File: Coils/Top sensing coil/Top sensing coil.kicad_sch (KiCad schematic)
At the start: 6 parts, among them J1 Conn_01x02_Pin, J2 Conn_01x02_Socket

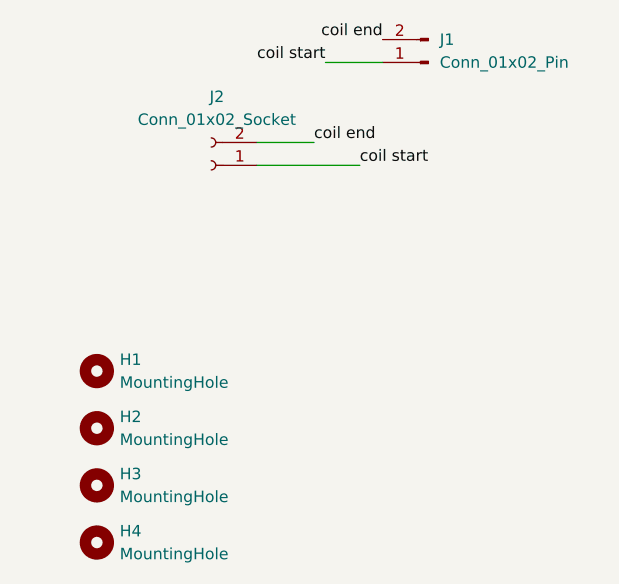
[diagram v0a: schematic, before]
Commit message: added 3d models for OPA3692, THS3091 and BNC connector
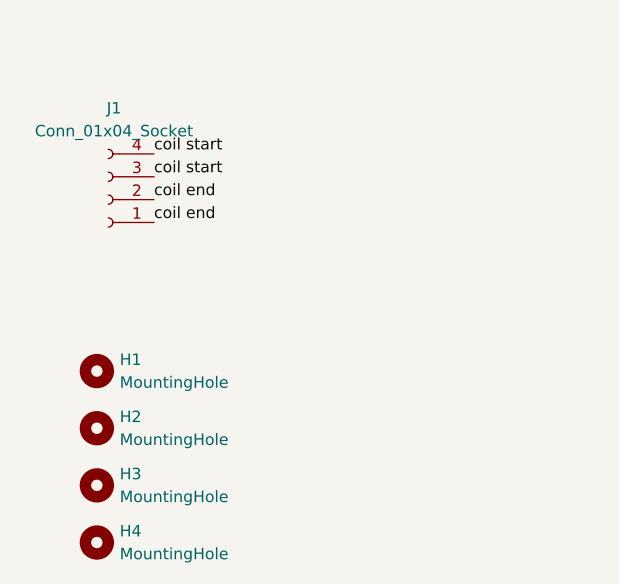
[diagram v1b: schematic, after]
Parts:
- removed J1: Conn_01x02_Pin, Connector_PinHeader_2.54mm:PinHeader_1x02_P2.54mm_Vertical, symbol Connector:Conn_01x02_Pin
- removed J2: Conn_01x02_Socket, Connector_PinSocket_2.54mm:PinSocket_1x02_P2.54mm_Vertical, symbol Connector:Conn_01x02_Socket
- added J1: Conn_01x04_Socket, Connector_PinSocket_2.54mm:PinSocket_1x04_P2.54mm_Horizontal, symbol Connector:Conn_01x04_Socket
- H1, H2, H3, H4: footprint MountingHole:MountingHole_5mm_Pad -> MountingHole:MountingHole_3.2mm_M3_Pad
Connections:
- net coil end: now also J1.1 (Pin_1), J1.2 (Pin_2)
- net coil start: now also J1.3 (Pin_3), J1.4 (Pin_4)

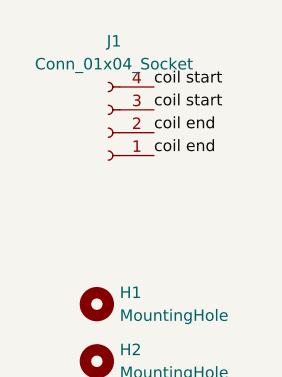
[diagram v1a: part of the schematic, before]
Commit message: Added via stiching to TX board, moved almost all vias off of pads, increased the trace width for the power supply and changed coil connector to horizontal socket
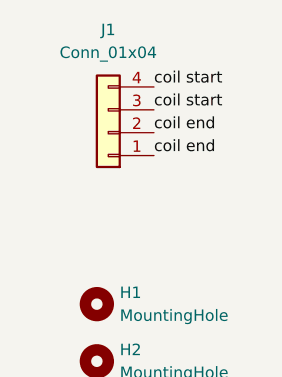
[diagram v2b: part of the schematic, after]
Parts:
- removed J1: Conn_01x04_Socket, Connector_PinSocket_2.54mm:PinSocket_1x04_P2.54mm_Horizontal, symbol Connector:Conn_01x04_Socket
- added J1: Conn_01x04, Connector_PinHeader_2.54mm:PinHeader_1x04_P2.54mm_Horizontal, symbol Connector_Generic:Conn_01x04
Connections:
- net coil end: now also J1.1 (Pin_1), J1.2 (Pin_2)
- net coil start: now also J1.3 (Pin_3), J1.4 (Pin_4)
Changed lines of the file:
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@@
 	)
 	(symbol
-		(lib_id "Connector:Conn_01x04_Socket")
+		(lib_id "Mechanical:MountingHole")
+		(at 41.91 86.36 0)
+		(unit 1)
+		(exclude_from_sim yes)
+		(in_bom no)
+		(on_board yes)
+		(dnp no)
+		(fields_autoplaced yes)
+		(property "Reference" "H3"
+			(at 44.45 85.0899 0)
+			(effects
+				(font
+					(size 1.27 1.27)
+				)
+				(justify left)
+			)
+		)
+		(property "Value" "MountingHole"
+			(at 44.45 87.6299 0)
+			(effects
+				(font
+					(size 1.27 1.27)
+				)
+				(justify left)
+			)
+		)
+		(property "Footprint" "MountingHole:MountingHole_3.2mm_M3_Pad"
+			(at 41.91 86.36 0)
+			(effects
+				(font
+					(size 1.27 1.27)
+				)
+				(hide yes)
+			)
+		)
+		(property "Datasheet" "~"
+			(at 41.91 86.36 0)
+			(effects
+				(font
+					(size 1.27 1.27)
+				)
+				(hide yes)
+			)
+		)
+		(property "Description" "Mounting Hole without connection"
+			(at 41.91 86.36 0)
+			(effects
+				(font
+					(size 1.27 1.27)
+				)
+				(hide yes)
+			)
+		)
+		(instances
+			(project "Top sensing coil"
+				(path "/fdf43bca-269e-4012-8925-740ac96f15da"
+					(reference "H3")
+					(unit 1)
+				)
+			)
+		)
+	)
+	(symbol
+		(lib_id "Mechanical:MountingHole")
+		(at 41.91 80.01 0)
+		(unit 1)
+		(exclude_from_sim yes)
+		(in_bom no)
+		(on_board yes)
+		(dnp no)
+		(fields_autoplaced yes)
+		(property "Reference" "H2"
+			(at 44.45 78.7399 0)
+			(effects
+				(font
+					(size 1.27 1.27)
+				)
+				(justify left)
+			)
+		)
+		(property "Value" "MountingHole"
+			(at 44.45 81.2799 0)
+			(effects
+				(font
+					(size 1.27 1.27)
+				)
+				(justify left)
+			)
+		)
+		(property "Footprint" "MountingHole:MountingHole_3.2mm_M3_Pad"
+			(at 41.91 80.01 0)
+			(effects
+				(font
+					(size 1.27 1.27)
+				)
+				(hide yes)
+			)
+		)
+		(property "Datasheet" "~"
+			(at 41.91 80.01 0)
+			(effects
+				(font
+					(size 1.27 1.27)
+				)
+				(hide yes)
+			)
+		)
+		(property "Description" "Mounting Hole without connection"
+			(at 41.91 80.01 0)
+			(effects
+				(font
+					(size 1.27 1.27)
+				)
+				(hide yes)
+			)
+		)
+		(instances
+			(project "Top sensing coil"
+				(path "/fdf43bca-269e-4012-8925-740ac96f15da"
+					(reference "H2")
+					(unit 1)
+				)
+			)
+		)
+	)
+	(symbol
+		(lib_id "Mechanical:MountingHole")
+		(at 41.91 92.71 0)
+		(unit 1)
+		(exclude_from_sim yes)
+		(in_bom no)
+		(on_board yes)
+		(dnp no)
+		(fields_autoplaced yes)
+		(property "Reference" "H4"
+			(at 44.45 91.4399 0)
+			(effects
+				(font
+					(size 1.27 1.27)
+				)
+				(justify left)
+			)
+		)
+		(property "Value" "MountingHole"
+			(at 44.45 93.9799 0)
+			(effects
+				(font
+					(size 1.27 1.27)
+				)
+				(justify left)
+			)
+		)
+		(property "Footprint" "MountingHole:MountingHole_3.2mm_M3_Pad"
+			(at 41.91 92.71 0)
+			(effects
+				(font
+					(size 1.27 1.27)
+				)
+				(hide yes)
+			)
+		)
+		(property "Datasheet" "~"
+			(at 41.91 92.71 0)
+			(effects
+				(font
+					(size 1.27 1.27)
+				)
+				(hide yes)
+			)
+		)
+		(property "Description" "Mounting Hole without connection"
+			(at 41.91 92.71 0)
+			(effects
+				(font
+					(size 1.27 1.27)
+				)
+				(hide yes)
+			)
+		)
+		(instances
+			(project "Top sensing coil"
+				(path "/fdf43bca-269e-4012-8925-740ac96f15da"
+					(reference "H4")
+					(unit 1)
+				)
+			)
+		)
+	)
+	(symbol
+		(lib_id "Connector_Generic:Conn_01x04")
 		(at 43.18 54.61 180)
 		(unit 1)
@@
 		(fields_autoplaced yes)
 		(property "Reference" "J1"
-			(at 43.815 44.45 0)
-			(effects
-				(font
-					(size 1.27 1.27)
-				)
-			)
-		)
-		(property "Value" "Conn_01x04_Socket"
-			(at 43.815 46.99 0)
-			(effects
-				(font
-					(size 1.27 1.27)
-				)
-			)
-		)
-		(property "Footprint" "Connector_PinSocket_2.54mm:PinSocket_1x04_P2.54mm_Horizontal"
+			(at 43.18 43.18 0)
+			(effects
+				(font
+					(size 1.27 1.27)
+				)
+			)
+		)
+		(property "Value" "Conn_01x04"
+			(at 43.18 45.72 0)
+			(effects
+				(font
+					(size 1.27 1.27)
+				)
+			)
+		)
+		(property "Footprint" "Connector_PinHeader_2.54mm:PinHeader_1x04_P2.54mm_Horizontal"
 			(at 43.18 54.61 0)
 			(effects
@@
 			)
 		)
-		(property "Description" "Generic connector, single row, 01x04, script generated"
+		(property "Description" "Generic connector, single row, 01x04, script generated (kicad-library-utils/schlib/autogen/connector/)"
 			(at 43.18 54.61 0)
 			(effects
@@
 			)
 		)
+		(pin "2"
+		)
 		(pin "1"
 		)
 		(pin "4"
 		)
-		(pin "2"
-		)
 		(pin "3"
 		)
@@
 					(unit 1)
 				)
-			)
-		)
-	)
-	(symbol
-		(lib_id "Mechanical:MountingHole")
-		(at 41.91 86.36 0)
-		(unit 1)
-		(exclude_from_sim yes)
-		(in_bom no)
-		(on_board yes)
-		(dnp no)
-		(fields_autoplaced yes)
-		(property "Reference" "H3"
-			(at 44.45 85.0899 0)
-			(effects
-				(font
-					(size 1.27 1.27)
-				)
-				(justify left)
-			)
-		)
-		(property "Value" "MountingHole"
-			(at 44.45 87.6299 0)
-			(effects
-				(font
-					(size 1.27 1.27)
-				)
-				(justify left)
-			)
-		)
-		(property "Footprint" "MountingHole:MountingHole_3.2mm_M3_Pad"
-			(at 41.91 86.36 0)
-			(effects
-				(font
-					(size 1.27 1.27)
-				)
-				(hide yes)
-			)
-		)
-		(property "Datasheet" "~"
-			(at 41.91 86.36 0)
-			(effects
-				(font
-					(size 1.27 1.27)
-				)
-				(hide yes)
-			)
-		)
-		(property "Description" "Mounting Hole without connection"
-			(at 41.91 86.36 0)
-			(effects
-				(font
-					(size 1.27 1.27)
-				)
-				(hide yes)
-			)
-		)
-		(instances
-			(project "Top sensing coil"
-				(path "/fdf43bca-269e-4012-8925-740ac96f15da"
-					(reference "H3")
-					(unit 1)
-				)
-			)
-		)
-	)
-	(symbol
-		(lib_id "Mechanical:MountingHole")
-		(at 41.91 80.01 0)
-		(unit 1)
-		(exclude_from_sim yes)
-		(in_bom no)
-		(on_board yes)
-		(dnp no)
-		(fields_autoplaced yes)
-		(property "Reference" "H2"
-			(at 44.45 78.7399 0)
-			(effects
-				(font
-					(size 1.27 1.27)
-				)
-				(justify left)
-			)
-		)
-		(property "Value" "MountingHole"
-			(at 44.45 81.2799 0)
-			(effects
-				(font
-					(size 1.27 1.27)
-				)
-				(justify left)
-			)
-		)
-		(property "Footprint" "MountingHole:MountingHole_3.2mm_M3_Pad"
-			(at 41.91 80.01 0)
-			(effects
-				(font
-					(size 1.27 1.27)
-				)
-				(hide yes)
-			)
-		)
-		(property "Datasheet" "~"
-			(at 41.91 80.01 0)
-			(effects
-				(font
-					(size 1.27 1.27)
-				)
-				(hide yes)
-			)
-		)
-		(property "Description" "Mounting Hole without connection"
-			(at 41.91 80.01 0)
-			(effects
-				(font
-					(size 1.27 1.27)
-				)
-				(hide yes)
-			)
-		)
-		(instances
-			(project "Top sensing coil"
-				(path "/fdf43bca-269e-4012-8925-740ac96f15da"
-					(reference "H2")
-					(unit 1)
-				)
-			)
-		)
-	)
-	(symbol
-		(lib_id "Mechanical:MountingHole")
-		(at 41.91 92.71 0)
-		(unit 1)
-		(exclude_from_sim yes)
-		(in_bom no)
-		(on_board yes)
-		(dnp no)
-		(fields_autoplaced yes)
-		(property "Reference" "H4"
-			(at 44.45 91.4399 0)
-			(effects
-				(font
-					(size 1.27 1.27)
-				)
-				(justify left)
-			)
-		)
-		(property "Value" "MountingHole"
-			(at 44.45 93.9799 0)
-			(effects
-				(font
-					(size 1.27 1.27)
-				)
-				(justify left)
-			)
-		)
-		(property "Footprint" "MountingHole:MountingHole_3.2mm_M3_Pad"
-			(at 41.91 92.71 0)
-			(effects
-				(font
-					(size 1.27 1.27)
-				)
-				(hide yes)
-			)
-		)
-		(property "Datasheet" "~"
-			(at 41.91 92.71 0)
-			(effects
-				(font
-					(size 1.27 1.27)
-				)
-				(hide yes)
-			)
-		)
-		(property "Description" "Mounting Hole without connection"
-			(at 41.91 92.71 0)
-			(effects
-				(font
-					(size 1.27 1.27)
-				)
-				(hide yes)
-			)
-		)
-		(instances
-			(project "Top sensing coil"
-				(path "/fdf43bca-269e-4012-8925-740ac96f15da"
-					(reference "H4")
-					(unit 1)
-				)
